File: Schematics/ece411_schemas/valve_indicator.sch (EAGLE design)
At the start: 87 parts, among them Q1 PMV45EN2R, Q2 PMV45EN2R, Q3 PMV45EN2R, Q4 PMV45EN2R, U1 AZ34063UMTR-G1, U2 AZ34063UMTR-G1, U3 STM32F042K6

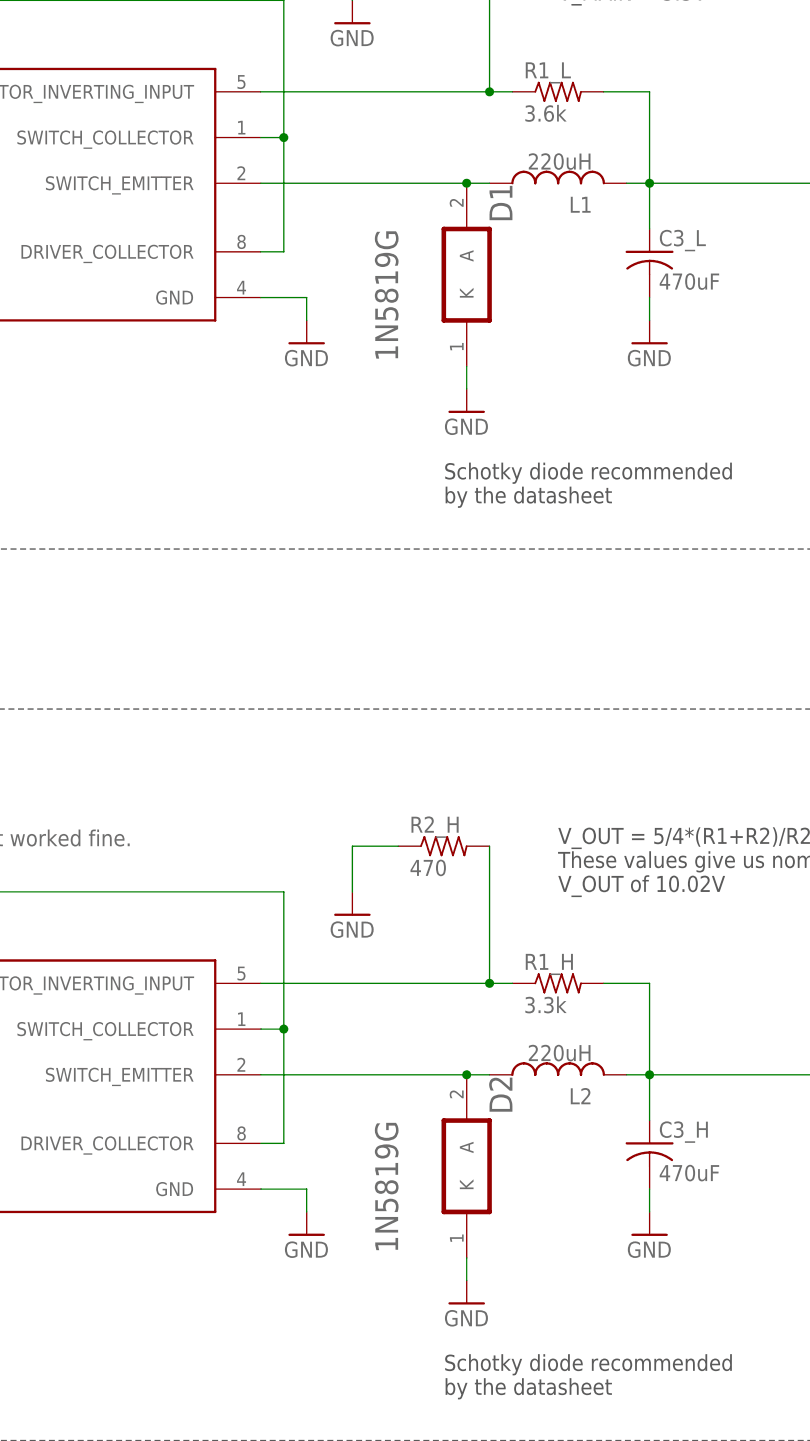
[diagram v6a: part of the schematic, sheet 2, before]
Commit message: updates to spacing on boards
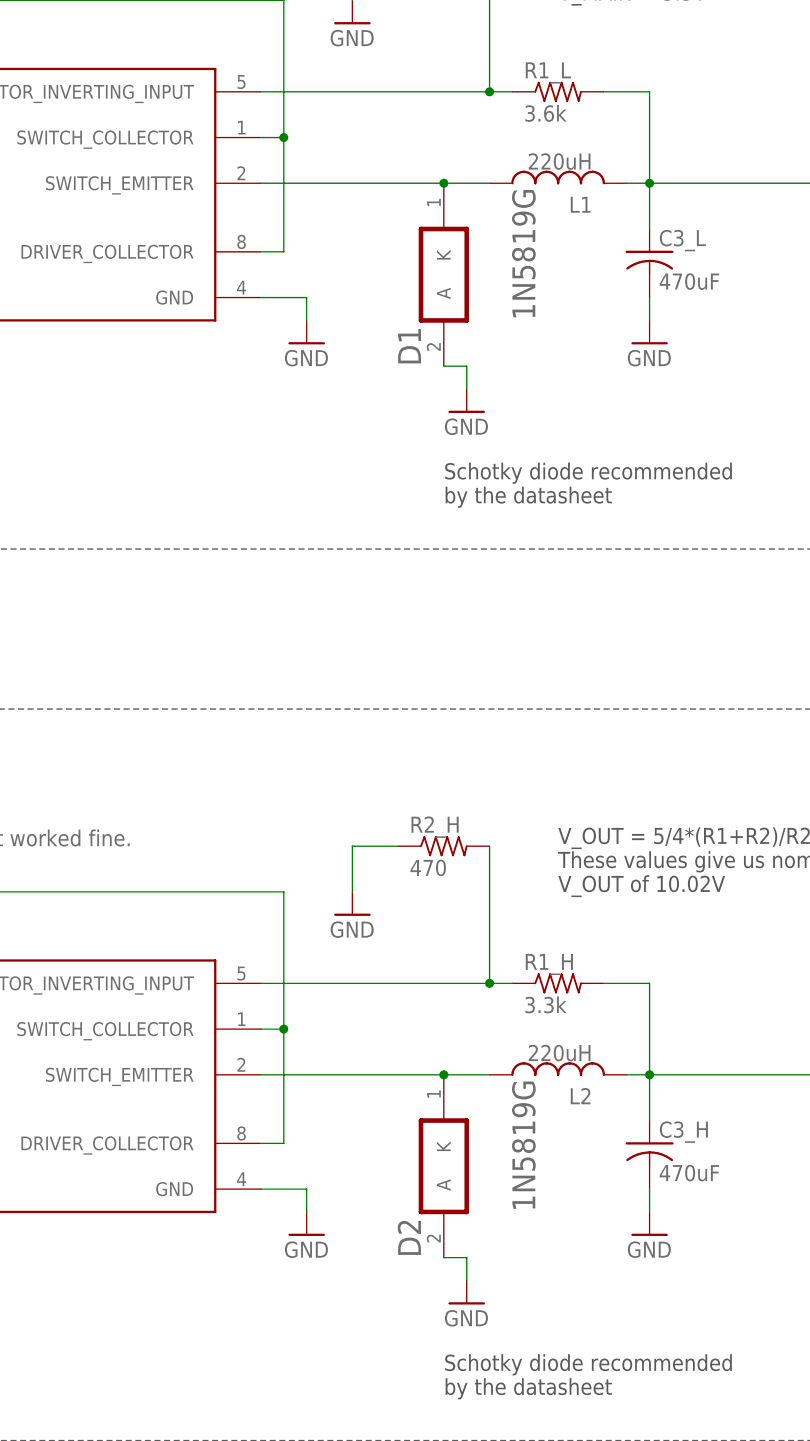
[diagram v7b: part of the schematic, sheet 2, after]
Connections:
- removed net N$21: D2.A, L2.1, U2.SWITCH_EMITTER
- new net N$10: D2.K, L2.1, U2.SWITCH_EMITTER
- net GND: now also D1.A, D2.A; no longer D1.K, D2.K
- net N$5: now also D1.K; no longer D1.A
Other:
- moved on the sheet: D1, D2
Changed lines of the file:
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@@
 <attribute name="VALUE" x="93.98" y="200.66" size="1.778" layer="96"/>
 </instance>
-<instance part="D1" gate="G$0" x="254" y="198.12" smashed="yes" rot="R270">
-<attribute name="NAME" x="251.46" y="203.2" size="2.54" layer="95" rot="R270" align="top-left"/>
-<attribute name="DIS" x="254" y="198.12" size="1.778" layer="96" rot="R270" display="off"/>
-<attribute name="DPN" x="254" y="198.12" size="1.778" layer="96" rot="R270" display="off"/>
-<attribute name="MFR" x="254" y="198.12" size="1.778" layer="96" rot="R270" display="off"/>
+<instance part="D1" gate="G$0" x="236.22" y="187.96" smashed="yes" rot="R90">
+<attribute name="NAME" x="238.76" y="182.88" size="2.54" layer="95" rot="R90" align="top-left"/>
+<attribute name="DIS" x="236.22" y="187.96" size="1.778" layer="96" rot="R90" display="off"/>
+<attribute name="DPN" x="236.22" y="187.96" size="1.778" layer="96" rot="R90" display="off"/>
+<attribute name="MFR" x="236.22" y="187.96" size="1.778" layer="96" rot="R90" display="off"/>
 </instance>
 <instance part="GND17" gate="1" x="246.38" y="177.8" smashed="yes">
@@
 <attribute name="VALUE" x="119.38" y="96.52" size="1.778" layer="96"/>
 </instance>
-<instance part="D2" gate="G$0" x="254" y="99.06" smashed="yes" rot="R270">
-<attribute name="NAME" x="251.46" y="104.14" size="2.54" layer="95" rot="R270" align="top-left"/>
-<attribute name="MFR" x="254" y="99.06" size="1.778" layer="96" rot="R270" display="off"/>
-<attribute name="DPN" x="254" y="99.06" size="1.778" layer="96" rot="R270" display="off"/>
-<attribute name="DIS" x="254" y="99.06" size="1.778" layer="96" rot="R270" display="off"/>
+<instance part="D2" gate="G$0" x="236.22" y="88.9" smashed="yes" rot="R90">
+<attribute name="NAME" x="238.76" y="83.82" size="2.54" layer="95" rot="R90" align="top-left"/>
+<attribute name="MFR" x="236.22" y="88.9" size="1.778" layer="96" rot="R90" display="off"/>
+<attribute name="DPN" x="236.22" y="88.9" size="1.778" layer="96" rot="R90" display="off"/>
+<attribute name="DIS" x="236.22" y="88.9" size="1.778" layer="96" rot="R90" display="off"/>
 </instance>
 <instance part="GND24" gate="1" x="246.38" y="78.74" smashed="yes">
@@
 </segment>
 <segment>
-<pinref part="D1" gate="G$0" pin="K"/>
-<pinref part="GND17" gate="1" pin="GND"/>
-<wire x1="246.38" y1="182.88" x2="246.38" y2="180.34" width="0.1524" layer="91"/>
-</segment>
-<segment>
 <pinref part="GND13" gate="1" pin="GND"/>
 <wire x1="266.7" y1="190.5" x2="266.7" y2="187.96" width="0.1524" layer="91"/>
@@
 </segment>
 <segment>
-<pinref part="D2" gate="G$0" pin="K"/>
-<pinref part="GND24" gate="1" pin="GND"/>
-<wire x1="246.38" y1="83.82" x2="246.38" y2="81.28" width="0.1524" layer="91"/>
-</segment>
-<segment>
 <pinref part="GND20" gate="1" pin="GND"/>
 <wire x1="266.7" y1="91.44" x2="266.7" y2="88.9" width="0.1524" layer="91"/>
@@
 <wire x1="15.24" y1="172.72" x2="15.24" y2="157.48" width="0.1524" layer="91"/>
 <pinref part="BATT" gate="G$1" pin="2"/>
+</segment>
+<segment>
+<pinref part="D1" gate="G$0" pin="A"/>
+<pinref part="GND17" gate="1" pin="GND"/>
+<wire x1="243.84" y1="182.88" x2="246.38" y2="182.88" width="0.1524" layer="91"/>
+<wire x1="246.38" y1="182.88" x2="246.38" y2="180.34" width="0.1524" layer="91"/>
+</segment>
+<segment>
+<pinref part="D2" gate="G$0" pin="A"/>
+<pinref part="GND24" gate="1" pin="GND"/>
+<wire x1="243.84" y1="83.82" x2="246.38" y2="83.82" width="0.1524" layer="91"/>
+<wire x1="246.38" y1="83.82" x2="246.38" y2="81.28" width="0.1524" layer="91"/>
 </segment>
 </net>
@@
 </segment>
 </net>
-<net name="N$5" class="0">
-<segment>
-<pinref part="D1" gate="G$0" pin="A"/>
-<pinref part="L1" gate="G$1" pin="1"/>
-<wire x1="248.92" y1="203.2" x2="246.38" y2="203.2" width="0.1524" layer="91"/>
-<pinref part="U1" gate="G$0" pin="SWITCH_EMITTER"/>
-<wire x1="223.52" y1="203.2" x2="246.38" y2="203.2" width="0.1524" layer="91"/>
-<junction x="246.38" y="203.2"/>
-</segment>
-</net>
 <net name="N$18" class="0">
 <segment>
@@
 <pinref part="R2_H" gate="G$1" pin="2"/>
 <pinref part="R1_H" gate="G$1" pin="1"/>
-</segment>
-</net>
-<net name="N$21" class="0">
-<segment>
-<pinref part="D2" gate="G$0" pin="A"/>
-<pinref part="L2" gate="G$1" pin="1"/>
-<wire x1="248.92" y1="104.14" x2="246.38" y2="104.14" width="0.1524" layer="91"/>
-<pinref part="U2" gate="G$0" pin="SWITCH_EMITTER"/>
-<wire x1="223.52" y1="104.14" x2="246.38" y2="104.14" width="0.1524" layer="91"/>
-<junction x="246.38" y="104.14"/>
 </segment>
 </net>
@@
 </segment>
 </net>
+<net name="N$5" class="0">
+<segment>
+<pinref part="U1" gate="G$0" pin="SWITCH_EMITTER"/>
+<pinref part="D1" gate="G$0" pin="K"/>
+<wire x1="223.52" y1="203.2" x2="243.84" y2="203.2" width="0.1524" layer="91"/>
+<pinref part="L1" gate="G$1" pin="1"/>
+<wire x1="243.84" y1="203.2" x2="248.92" y2="203.2" width="0.1524" layer="91"/>
+<junction x="243.84" y="203.2"/>
+</segment>
+</net>
+<net name="N$10" class="0">
+<segment>
+<pinref part="U2" gate="G$0" pin="SWITCH_EMITTER"/>
+<pinref part="D2" gate="G$0" pin="K"/>
+<wire x1="223.52" y1="104.14" x2="243.84" y2="104.14" width="0.1524" layer="91"/>
+<pinref part="L2" gate="G$1" pin="1"/>
+<wire x1="243.84" y1="104.14" x2="248.92" y2="104.14" width="0.1524" layer="91"/>
+<junction x="243.84" y="104.14"/>
+</segment>
+</net>
